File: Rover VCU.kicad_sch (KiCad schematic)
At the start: 6 parts, among them J3 430450400, J6 430451200

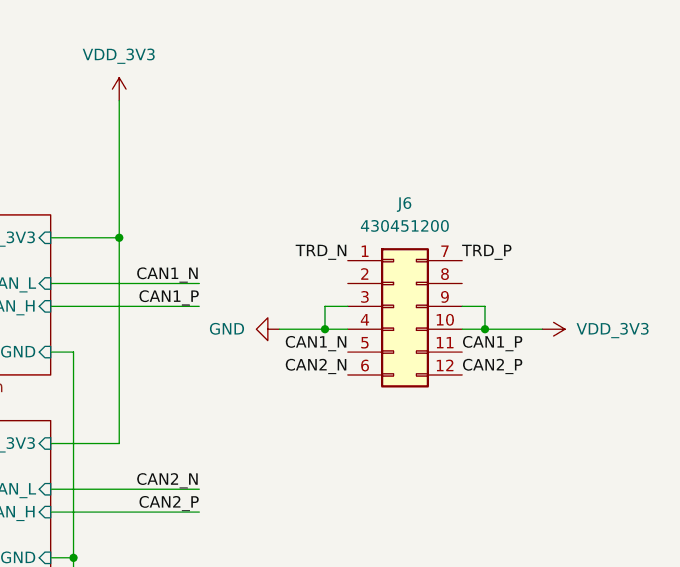
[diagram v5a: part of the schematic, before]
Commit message: fix: cleaned up DRC and ERC's for major errors
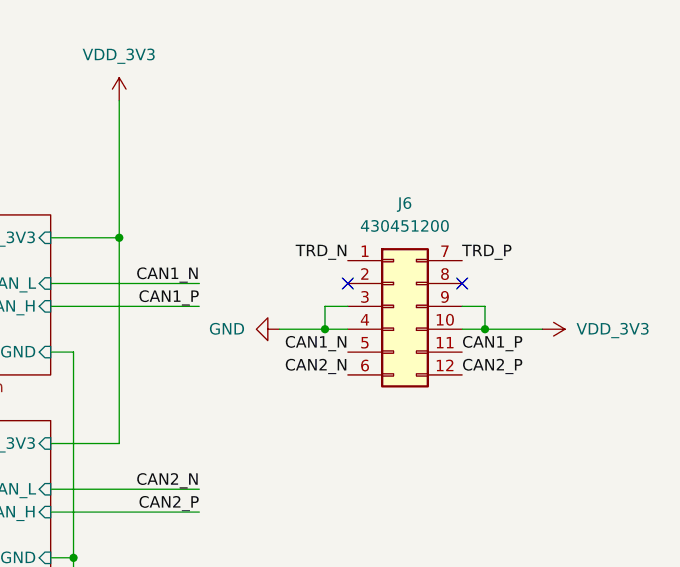
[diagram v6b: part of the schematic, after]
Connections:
- no-connect marks 0 -> 2
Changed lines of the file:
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@@
 	(paper "A4")
+	(junction
+		(at 86.36 55.88)
+		(diameter 0)
+		(color 0 0 0 0)
+	)
 	(junction
 		(at 214.63 88.9)
@@
 	)
 	(junction
-		(at 86.36 55.88)
-		(diameter 0)
-		(color 0 0 0 0)
-	)
-	(junction
 		(at 209.55 124.46)
 		(diameter 0)
@@
 		(diameter 0)
 		(color 0 0 0 0)
+	)
+	(no_connect
+		(at 240.03 93.98)
+	)
+	(no_connect
+		(at 252.73 93.98)
 	)
 	(wire
@@
 	)
 	(symbol
+		(lib_id "power:PWR_FLAG")
+		(at 86.36 55.88 270)
+		(unit 1)
+		(body_style 1)
+		(exclude_from_sim no)
+		(in_bom yes)
+		(on_board yes)
+		(in_pos_files yes)
+		(dnp no)
+		(fields_autoplaced yes)
+		(property "Reference" "#FLG02"
+			(at 88.265 55.88 0)
+			(hide yes)
+			(show_name no)
+			(do_not_autoplace no)
+			(effects
+				(font
+					(size 1.27 1.27)
+				)
+			)
+		)
+		(property "Value" "PWR_FLAG"
+			(at 90.17 55.8799 90)
+			(show_name no)
+			(do_not_autoplace no)
+			(effects
+				(font
+					(size 1.27 1.27)
+				)
+				(justify left)
+			)
+		)
+		(property "Footprint" ""
+			(at 86.36 55.88 0)
+			(hide yes)
+			(show_name no)
+			(do_not_autoplace no)
+			(effects
+				(font
+					(size 1.27 1.27)
+				)
+			)
+		)
+		(property "Datasheet" ""
+			(at 86.36 55.88 0)
+			(hide yes)
+			(show_name no)
+			(do_not_autoplace no)
+			(effects
+				(font
+					(size 1.27 1.27)
+				)
+			)
+		)
+		(property "Description" "Special symbol for telling ERC where power comes from"
+			(at 86.36 55.88 0)
+			(hide yes)
+			(show_name no)
+			(do_not_autoplace no)
+			(effects
+				(font
+					(size 1.27 1.27)
+				)
+			)
+		)
+		(pin "1"
+		)
+		(instances
+			(project "Rover VCU"
+				(path "/33c96268-4ca2-4a73-94d6-a3ed4f27d429"
+					(reference "#FLG02")
+					(unit 1)
+				)
+			)
+		)
+	)
+	(symbol
 		(lib_id "0_chenry_lib:VDD_3V3")
 		(at 261.62 99.06 270)
@@
 					(unit 1)
 				)
-			)
-		)
-	)
-	(symbol
-		(lib_id "power:PWR_FLAG")
-		(at 86.36 55.88 270)
-		(unit 1)
-		(body_style 1)
-		(exclude_from_sim no)
-		(in_bom yes)
-		(on_board yes)
-		(in_pos_files yes)
-		(dnp no)
-		(fields_autoplaced yes)
-		(property "Reference" "#FLG02"
-			(at 88.265 55.88 0)
-			(hide yes)
-			(show_name no)
-			(do_not_autoplace no)
-			(effects
-				(font
-					(size 1.27 1.27)
-				)
-			)
-		)
-		(property "Value" "PWR_FLAG"
-			(at 90.17 55.8799 90)
-			(show_name no)
-			(do_not_autoplace no)
-			(effects
-				(font
-					(size 1.27 1.27)
-				)
-				(justify left)
-			)
-		)
-		(property "Footprint" ""
-			(at 86.36 55.88 0)
-			(hide yes)
-			(show_name no)
-			(do_not_autoplace no)
-			(effects
-				(font
-					(size 1.27 1.27)
-				)
-			)
-		)
-		(property "Datasheet" ""
-			(at 86.36 55.88 0)
-			(hide yes)
-			(show_name no)
-			(do_not_autoplace no)
-			(effects
-				(font
-					(size 1.27 1.27)
-				)
-			)
-		)
-		(property "Description" "Special symbol for telling ERC where power comes from"
-			(at 86.36 55.88 0)
-			(hide yes)
-			(show_name no)
-			(do_not_autoplace no)
-			(effects
-				(font
-					(size 1.27 1.27)
-				)
-			)
-		)
-		(pin "1"
-		)
-		(instances
-			(project "Rover VCU"
-				(path "/33c96268-4ca2-4a73-94d6-a3ed4f27d429"
-					(reference "#FLG02")
-					(unit 1)
-				)

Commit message: fix: final polishes for MFR
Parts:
- H1, H2, H3, H4: footprint MountingHole:MountingHole_3.5mm -> (none)

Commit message: fix: added annotations and 3d models
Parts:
- J6: footprint Connector_Molex:Molex_Micro-Fit_3.0_43045-1221_2x06-1MP_P3.00mm_Horizontal -> Connector_Molex:Molex_Micro-Fit_3.0_43045-1200_2x06_P3.00mm_Horizontal
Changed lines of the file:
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@@
 			)
 		)
-		(property "Footprint" "Connector_Molex:Molex_Micro-Fit_3.0_43045-1221_2x06-1MP_P3.00mm_Horizontal"
+		(property "Footprint" "Connector_Molex:Molex_Micro-Fit_3.0_43045-1200_2x06_P3.00mm_Horizontal"
 			(at 245.11 96.52 0)
 			(hide yes)
